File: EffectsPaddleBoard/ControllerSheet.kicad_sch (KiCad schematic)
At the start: 23 parts, among them J1 Conn_01x03_Pin, J2 Conn_01x06_Pin, J4 Conn_01x04_Pin, SW1 SW_SPDT, SW2 SW_Push, SW3 SW_SPDT, U1 STM32F405RGTx, Y1 16MHz

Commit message: Corrections, see comments
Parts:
- D1: Distributer Link (none) -> https://www.mouser.ch/ProductDetail/Wurth-Elektronik/150040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; Manufacturer (none) -> Wurth Elektronik; Manufacturer Part Number (none) -> 150040RS73240
- J1: Distributer Link (none) -> https://www.digikey.ch/en/products/detail/adam-tech/2PH1-03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; Manufacturer (none) -> Adam Tech; Manufacturer Part Number (none) -> 2PH1-03-UA
- R33: value 10k -> 220
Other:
- note added: "fc fitting"
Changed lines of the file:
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@@
     (effects (font (size 4 4)) (justify left bottom))
+  )
+  (text "fc fitting" (at 52.705 64.77 0)
+    (effects (font (size 1.27 1.27)) (justify left bottom))
   )
   (global_label "OSC_PH1" (shape input) (at 262.89 98.425 0) (fields_autoplaced)
@@
       (effects (font (size 1.27 1.27)))
     )
-    (property "Value" "10k" (at 43.18 66.04 90)
+    (property "Value" "220" (at 43.18 66.04 90)
       (effects (font (size 1.27 1.27)))
     )
@@
       (effects (font (size 1.27 1.27)) hide)
     )
-    (property "Distributer Link" "" (at 101.6 182.245 0)
-      (effects (font (size 1.27 1.27)) hide)
-    )
-    (property "Manufacturer" "" (at 101.6 182.245 0)
-      (effects (font (size 1.27 1.27)) hide)
-    )
-    (property "Manufacturer Part Number" "" (at 101.6 182.245 0)
+    (property "Distributer Link" "https://www.mouser.ch/ProductDetail/Wurth-Elektronik/150040RS73240?qs=8Aam6%252B7C6HGMiInmnlrBiw%3D%3D" (at 101.6 182.245 0)
+      (effects (font (size 1.27 1.27)) hide)
+    )
+    (property "Manufacturer" "Wurth Elektronik" (at 101.6 182.245 0)
+      (effects (font (size 1.27 1.27)) hide)
+    )
+    (property "Manufacturer Part Number" "150040RS73240" (at 101.6 182.245 0)
       (effects (font (size 1.27 1.27)) hide)
     )
@@
       (effects (font (size 1.27 1.27)) hide)
     )
-    (property "Distributer Link" "" (at 24.765 182.88 0)
-      (effects (font (size 1.27 1.27)) hide)
-    )
-    (property "Manufacturer" "" (at 24.765 182.88 0)
-      (effects (font (size 1.27 1.27)) hide)
-    )
-    (property "Manufacturer Part Number" "" (at 24.765 182.88 0)
-      (effects (font (size 1.27 1.27)) hide)
-    )
+    (property "Distributer Link" "https://www.digikey.ch/en/products/detail/adam-tech/2PH1-03-UA/9830409" (at 24.765 182.88 0)
+      (effects (font (size 1.27 1.27)) hide)
+    )
+    (property "Manufacturer" "Adam Tech" (at 24.765 182.88 0)
+      (effects (font (size 1.27 1.27)) hide)
+    )
+    (property "Manufacturer Part Number" "2PH1-03-UA" (at 24.765 182.88 0)
+      (effects (font (size 1.27 1.27)) hide)
+    )

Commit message: Corrected the board, now all parts should be right
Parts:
- C6: footprint Capacitor_SMD:C_1206_3216Metric -> Capacitor_SMD:C_0805_2012Metric
- C8: value 100n -> 1u; footprint Capacitor_SMD:C_0402_1005Metric -> Capacitor_SMD:C_0805_2012Metric
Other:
- note removed: "fc fitting"
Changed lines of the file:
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@@
     (effects (font (size 4 4)) (justify left bottom))
-  )
-  (text "fc fitting" (at 52.705 64.77 0)
-    (effects (font (size 1.27 1.27)) (justify left bottom))
   )
   (global_label "OSC_PH1" (shape input) (at 262.89 98.425 0) (fields_autoplaced)
@@
       (effects (font (size 1.27 1.27)) (justify left))
     )
-    (property "Value" "100n" (at 62.865 74.295 0)
-      (effects (font (size 1.27 1.27)) (justify left))
-    )
-    (property "Footprint" "Capacitor_SMD:C_0402_1005Metric" (at 60.0202 76.2 0)
+    (property "Value" "1u" (at 62.865 74.295 0)
+      (effects (font (size 1.27 1.27)) (justify left))
+    )
+    (property "Footprint" "Capacitor_SMD:C_0805_2012Metric" (at 60.0202 76.2 0)
       (effects (font (size 1.27 1.27)) hide)
     )
@@
       (effects (font (size 1.27 1.27)) (justify left))
     )
-    (property "Footprint" "Capacitor_SMD:C_1206_3216Metric" (at 27.6352 44.45 0)
-      (effects (font (size 1.27 1.27)) hide)
-    )
+    (property "Footprint" "Capacitor_SMD:C_0805_2012Metric" (at 27.6352 44.45 0)
+      (effects (font (size 1.27 1.27)) hide)
+    )

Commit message: Added all parts
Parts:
- C1, C2, C3, C4, C5, C7: Distributer Link https://www.mouser.ch/ProductDetail/Murata-Electronics/GRM152R61A104KE19D?qs=IPQhFcwEUOjgOs7G%2Fz457g%3D%3D -> https://www.mouser.ch/ProductDetail/Murata-Electronics/GRM155R61C104KA88J?qs=sGAEpiMZZMsh%252B1woXyUXj8YF%2FGivH5Kx4uStnYyl8jU%3D; Manufacturer Part Number GRM152R61A104KE19D -> GRM155R61C104KA88J
- C6: Distributer Link https://www.mouser.ch/ProductDetail/Murata-Electronics/GRM3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 -> https://www.mouser.ch/ProductDetail/Murata-Electronics/GCM2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; Manufacturer Part Number GRM31CR71C106KAC7L -> GCM21BC71E106KE36K
- C8: Distributer Link https://www.mouser.ch/ProductDetail/Murata-Electronics/GRM1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 -> https://www.mouser.ch/ProductDetail/Murata-Electronics/GRM2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; Manufacturer Part Number GRM152R61A104KE19D -> GRM21BR71C105KA01K
- J1, J2, J4: now not fitted; now left out of the parts list
- R1, R34: Distributer Link (none) -> https://www.mouser.ch/ProductDetail/Vishay-Beyschlag/MCS040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; Manufacturer (none) -> Vishay / Beyschlag; Manufacturer Part Number (none) -> MCS04020D1002BE000
- R2, R33: Distributer Link (none) -> https://www.mouser.ch/ProductDetail/Vishay-Beyschlag/MCS040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; Manufacturer (none) -> Vishay / Beyschlag; Manufacturer Part Number (none) -> MCS04020C2200FE000
- SW1, SW3: Distributer Link (none) -> https://www.mouser.ch/ProductDetail/CK/PCM12SMTR?qs=mfFuHy8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; Manufacturer (none) -> C&K; Manufacturer Part Number (none) -> PCM12SMTR
- SW2: Distributer Link (none) -> https://www.mouser.ch/ProductDetail/Omron-Electronics/B3S-1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; Manufacturer (none) -> Omron Electronics; Manufacturer Part Number (none) -> B3S-1000
- U1: Distributer Link (none) -> https://www.mouser.ch/ProductDetail/STMicroelectronics/STM3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; Manufacturer (none) -> STMicroelectronics; Manufacturer Part Number (none) -> STM32F405RGT7
- Y1: Distributer Link (none) -> https://www.mouser.ch/ProductDetail/Epson-Timing/SG3225CAN-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; Manufacturer (none) -> Epson Timing; Manufacturer Part Number (none) -> SG3225CAN 16.0000M-TJGA3

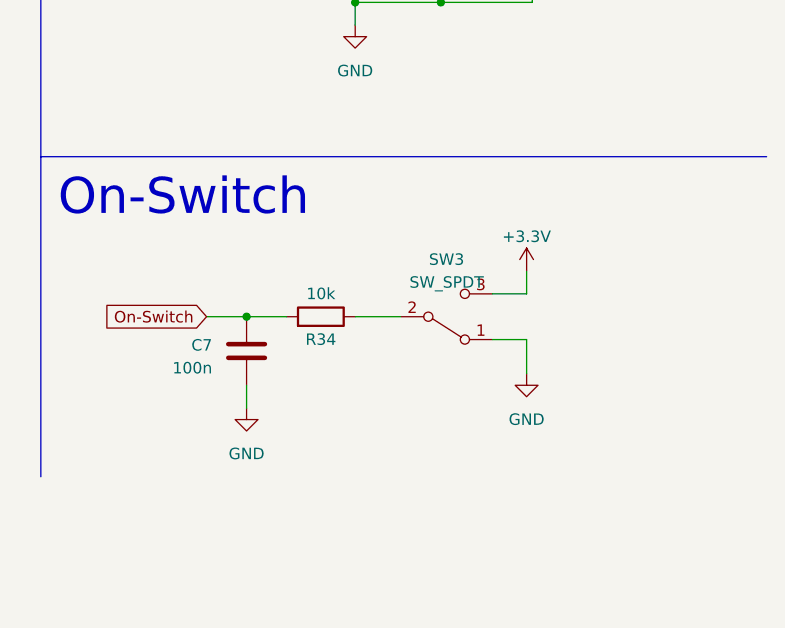
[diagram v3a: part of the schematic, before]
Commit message: Added final button footprint
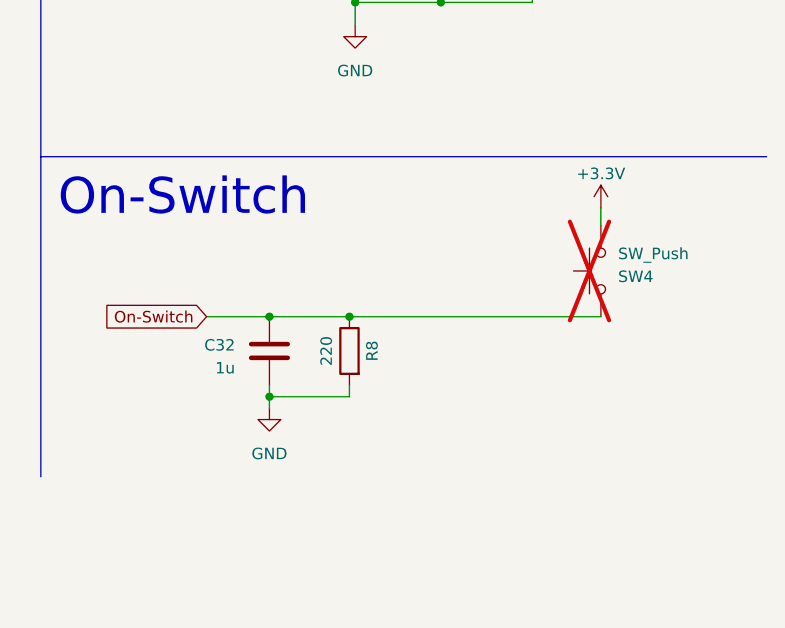
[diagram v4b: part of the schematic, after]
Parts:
- removed C7: 100n, Capacitor_SMD:C_0402_1005Metric, symbol Device:C
- removed R34: 10k, Resistor_SMD:R_0402_1005Metric, symbol Device:R
- removed SW3: SW_SPDT, Button_Switch_SMD:SW_SPDT_PCM12, symbol Switch:SW_SPDT
- added C32: 1u, Capacitor_SMD:C_0805_2012Metric, symbol Device:C
- added R8: 220, Resistor_SMD:R_0402_1005Metric, symbol Device:R
- added SW4: SW_Push, Button_Switch_THT:SW_CW_GPTS203211B, symbol Switch:SW_Push
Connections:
- net +3.3V: now also SW4.1
- net GND: now also C32.2, R8.2
- net On-Switch: now also C32.1, R8.1, SW4.2

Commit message: exported symbols and footprints, updated PCB
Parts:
- added C40: 10u, Capacitor_SMD:C_0805_2012Metric, symbol EffectsPaddleBoard:C
- added C7: 100n, Capacitor_SMD:C_0402_1005Metric, symbol EffectsPaddleBoard:C
- added R10: 220, Resistor_SMD:R_0402_1005Metric, symbol EffectsPaddleBoard:R
- C1, C10, C2, C3, C32, C4, C5, C6, C8, C9: symbol Device:C -> EffectsPaddleBoard:C
- D1: symbol Device:LED -> EffectsPaddleBoard:LED
- J1: symbol Connector:Conn_01x03_Pin -> EffectsPaddleBoard:Conn_01x03_Pin
- J2: symbol Connector:Conn_01x06_Pin -> EffectsPaddleBoard:Conn_01x06_Pin
- J4: symbol Connector:Conn_01x04_Pin -> EffectsPaddleBoard:Conn_01x04_Pin
- R1, R2, R33, R8: symbol Device:R -> EffectsPaddleBoard:R
- SW1: symbol Switch:SW_SPDT -> EffectsPaddleBoard:SW_SPDT
- SW2, SW4: symbol Switch:SW_Push -> EffectsPaddleBoard:SW_Push
- U1: symbol MCU_ST_STM32F4:STM32F405RGTx -> EffectsPaddleBoard:STM32F405RGTx
- Y1: symbol Device:Crystal_GND24 -> EffectsPaddleBoard:Crystal_GND24
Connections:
- net +3.3VA: now also C40.1, C7.1
- net GND: now also C40.2, C7.2, R10.1; no longer R8.2
- net On-Switch: now also R10.2; no longer SW4.2
- new net: R8.2, SW4.2
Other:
- moved on the sheet: C10, C32, C8, C9, D1, J1, J2, R2, R8, SW4, Y1

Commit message: Added new buck regulator, but footprint is missing
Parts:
- SW4: footprint Button_Switch_THT:SW_CW_GPTS203211B -> EffectsPaddleBoard:SW_DIP_SPSTx01_Piano_10.8x4.1mm_W7.62mm_P2.54mm
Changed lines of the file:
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@@
       (effects (font (size 1.27 1.27)) (justify right))
     )
-    (property "Footprint" "Button_Switch_THT:SW_CW_GPTS203211B" (at 261.62 143.51 0)
+    (property "Footprint" "EffectsPaddleBoard:SW_DIP_SPSTx01_Piano_10.8x4.1mm_W7.62mm_P2.54mm" (at 261.62 143.51 0)
       (effects (font (size 1.27 1.27)) hide)
     )

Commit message: Upgraded to kicad8 and improved layout
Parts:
- C1, C10, C2, C3, C4, C5, C7, C9: footprint Capacitor_SMD:C_0402_1005Metric -> Capacitor_SMD:C_0603_1608Metric
- D1: footprint LED_SMD:LED_0402_1005Metric -> LED_SMD:LED_0603_1608Metric
- J1: footprint Connector_PinHeader_2.00mm:PinHeader_1x03_P2.00mm_Vertical -> Connector_PinHeader_2.54mm:PinHeader_1x03_P2.54mm_Vertical
- J2: footprint Connector_PinHeader_2.00mm:PinHeader_1x06_P2.00mm_Vertical -> Connector_PinHeader_2.54mm:PinHeader_1x06_P2.54mm_Vertical
- J4: footprint Connector_PinHeader_2.00mm:PinHeader_1x04_P2.00mm_Vertical -> Connector_PinHeader_2.54mm:PinHeader_1x04_P2.54mm_Vertical
- R1, R10, R2, R33, R8: footprint Resistor_SMD:R_0402_1005Metric -> Resistor_SMD:R_0603_1608Metric

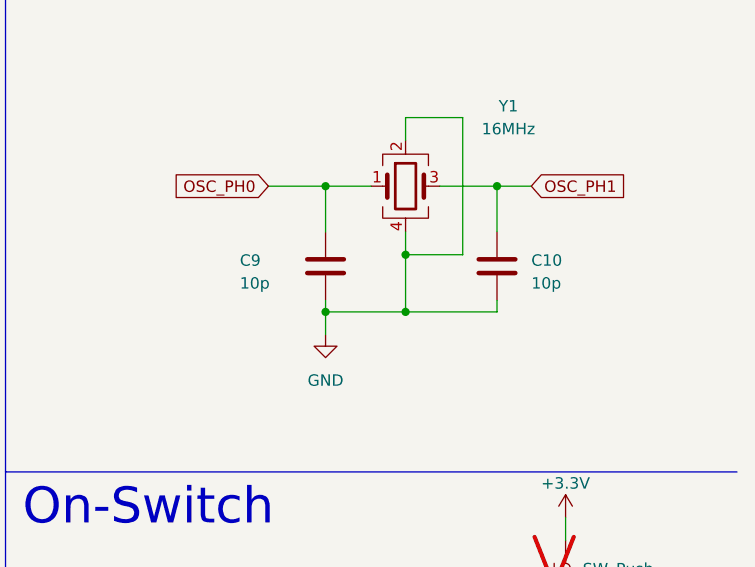
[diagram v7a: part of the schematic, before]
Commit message: Changed oscillator, not sure if this works
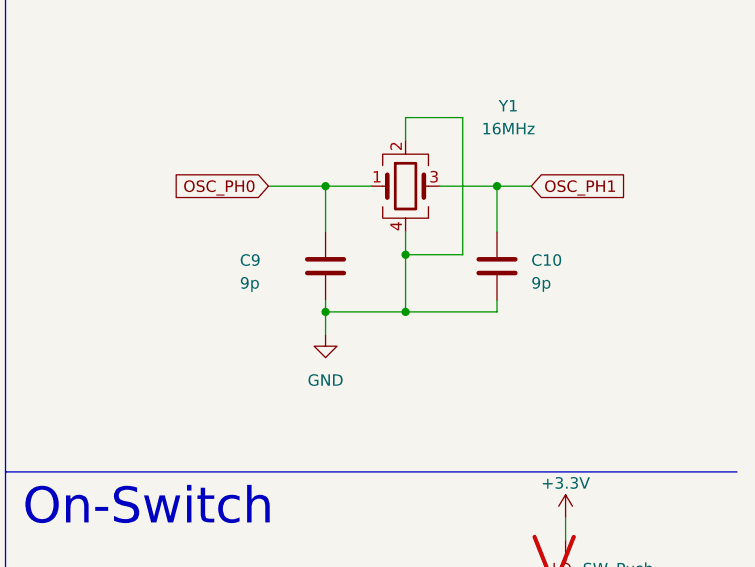
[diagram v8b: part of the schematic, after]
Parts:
- C10, C9: value 10p -> 9p
- Y1: Distributer Link https://www.mouser.ch/ProductDetail/Epson-Timing/SG3225CAN-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 -> https://www.mouser.ch/ProductDetail/ABRACON/ABM8-16000MHZ-B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; Manufacturer Epson Timing -> Abracon; Manufacturer Part Number SG3225CAN 16.0000M-TJGA3 -> ABM8-16.000MHZ-B2-T
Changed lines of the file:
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@@
 			)
 		)
-		(property "Distributer Link" "https://www.mouser.ch/ProductDetail/Epson-Timing/SG3225CAN-16.0000M-TJGA3?qs=W%2FMpXkg%252BdQ43Tw%252BixNK2Iw%3D%3D"
+		(property "Distributer Link" "https://www.mouser.ch/ProductDetail/ABRACON/ABM8-16000MHZ-B2-T?qs=H8AWquzS%2FlMP55oyx0gddg%3D%3D&mgh=1&utm_id=19994302035&gad_source=1&gclid=CjwKCAiAxaCvBhBaEiwAvsLmWNBqWPXTvfSak4t3wiz9syGwiagnBuou7zGS8mMES1DNn5A8_tbzQRoCKRIQAvD_BwE"
 			(at 248.92 99.06 0)
 			(effects
@@
 			)
 		)
-		(property "Manufacturer" "Epson Timing"
+		(property "Manufacturer" "Abracon"
 			(at 248.92 99.06 0)
 			(effects
@@
 			)
 		)
-		(property "Manufacturer Part Number" "SG3225CAN 16.0000M-TJGA3"
+		(property "Manufacturer Part Number" "ABM8-16.000MHZ-B2-T"
 			(at 248.92 99.06 0)
 			(effects
@@
 			)
 		)
-		(property "Value" "10p"
+		(property "Value" "9p"
 			(at 262.89 109.855 0)
 			(effects
@@
 			)
 		)
-		(property "Value" "10p"
+		(property "Value" "9p"
 			(at 230.505 109.855 0)
 			(effects
